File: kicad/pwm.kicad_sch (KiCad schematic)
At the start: 27 parts, among them J28 DC ports, J29 LED ports, J30 PCA9685 #1 ch 0, Q11 AO3400A, U7 PCA9685PW, U8 74HCT244D, U9 74HCT244D

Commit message: kicad: v2 space measures - feeder on power bar header, resistor arrays, 0603, TSSOP buffers
Feeder port dropped: power bar header pin 10 = +3V3_EXT (own AMS1117), any PCA #2 channel as signal; 30 series resistors as 8x 4x0603 arrays; new passives 0603; new 74HCT244 in TSSOP-20; flat parts may use the Pi zone, connectors anywhere else. ERC 0, DRC copper 0, parity 0.

Co-Authored-By: Claude Opus 5.5 <noreply@anthropic.com>
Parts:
- removed D29: SS54, Diode_SMD:D_SMA, symbol Device:D_Schottky
- removed J30: PCA9685 #1 ch 0, aquaPCB:TerminalBlock_Kangnex_WJ250B-3.5-03P_P3.50mm_Staggered, symbol Connector:Screw_Terminal_01x03
- removed Q11: AO3400A, Package_TO_SOT_SMD:SOT-23, symbol Transistor_FET:AO3400A
- removed R53, R54, R55, R56, R57, R58, R59, R60, R61, R62, R63, R64, R65, R66, R67: 100, Resistor_SMD:R_0805_2012Metric, symbol Device:R
- removed R68: 10k, Resistor_SMD:R_0805_2012Metric, symbol Device:R
- added RN1, RN2, RN3, RN4: 4x100, Resistor_SMD:R_Array_Convex_4x0603, symbol Device:R_Pack04
- C20, C21, C22: footprint Capacitor_SMD:C_0805_2012Metric -> Capacitor_SMD:C_0603_1608Metric; LCSC C49678 -> C14663
- U8, U9: value 74HCT244D -> 74HCT244PW; footprint Package_SO:SOIC-20W_7.5x12.8mm_P1.27mm -> Package_SO:TSSOP-20_4.4x6.5mm_P0.65mm; LCSC C5978 -> C131088
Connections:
- net DC_PWM1: now also RN1.8 (R1.2)
- net DC_PWM1_B: now also RN1.1 (R1.1)
- net DC_PWM2: now also RN1.7 (R2.2)
- net DC_PWM2_B: now also RN1.2 (R2.1)
- net DC_PWM3: now also RN1.6 (R3.2)
- net DC_PWM3_B: now also RN1.3 (R3.1)
- net DC_PWM4: now also RN1.5 (R4.2)
- net DC_PWM4_B: now also RN1.4 (R4.1)
- net DC_PWM6: now also RN2.8 (R1.2)
- net DC_PWM6_B: now also RN2.1 (R1.1)
- net DC_PWM7: now also RN2.7 (R2.2)
- net DC_PWM7_B: now also RN2.2 (R2.1)
- net DC_PWM9: now also RN2.6 (R3.2)
- net DC_PWM9_B: now also RN2.3 (R3.1)
- net LED_PWM10: now also RN3.7 (R2.2)
- net LED_PWM10_B: now also RN3.2 (R2.1)
- net LED_PWM11: now also RN3.6 (R3.2)
- net LED_PWM11_B: now also RN3.3 (R3.1)
- net LED_PWM12: now also RN3.5 (R4.2)
- net LED_PWM12_B: now also RN3.4 (R4.1)
- net LED_PWM13: now also RN4.8 (R1.2)
- net LED_PWM13_B: now also RN4.1 (R1.1)
- net LED_PWM14: now also RN4.7 (R2.2)
- net LED_PWM14_B: now also RN4.2 (R2.1)
- net LED_PWM15: now also RN4.6 (R3.2)
- net LED_PWM15_B: now also RN4.3 (R3.1)
- net LED_PWM8: now also RN3.8 (R1.2)
- net LED_PWM8_B: now also RN3.1 (R1.1)
- net PCA1_CH0: no longer names the net of U7.6 (LED0)
- no-connect marks 3 -> 8
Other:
- note added: "PCA9685 #1, I2C address 0x40. /OE fixed to GND: after power-on all outputs are LOW (datasheet 7.5); a Pi reboot does NOT reset the chip - outputs keep their state until software re-initialises it. LED0, LED5 = spare."
- note removed: "Feeder (Robo-Tank v3 order +3.3V / Signal / GND; Signal = switched ground, < 500 mA)"
- note removed: "PCA9685 #1, I2C address 0x40. /OE fixed to GND: after power-on all outputs are LOW (datasheet 7.5); a Pi reboot does NOT reset the chip - outputs keep their state until software re-initialises it. LED5 = spare."

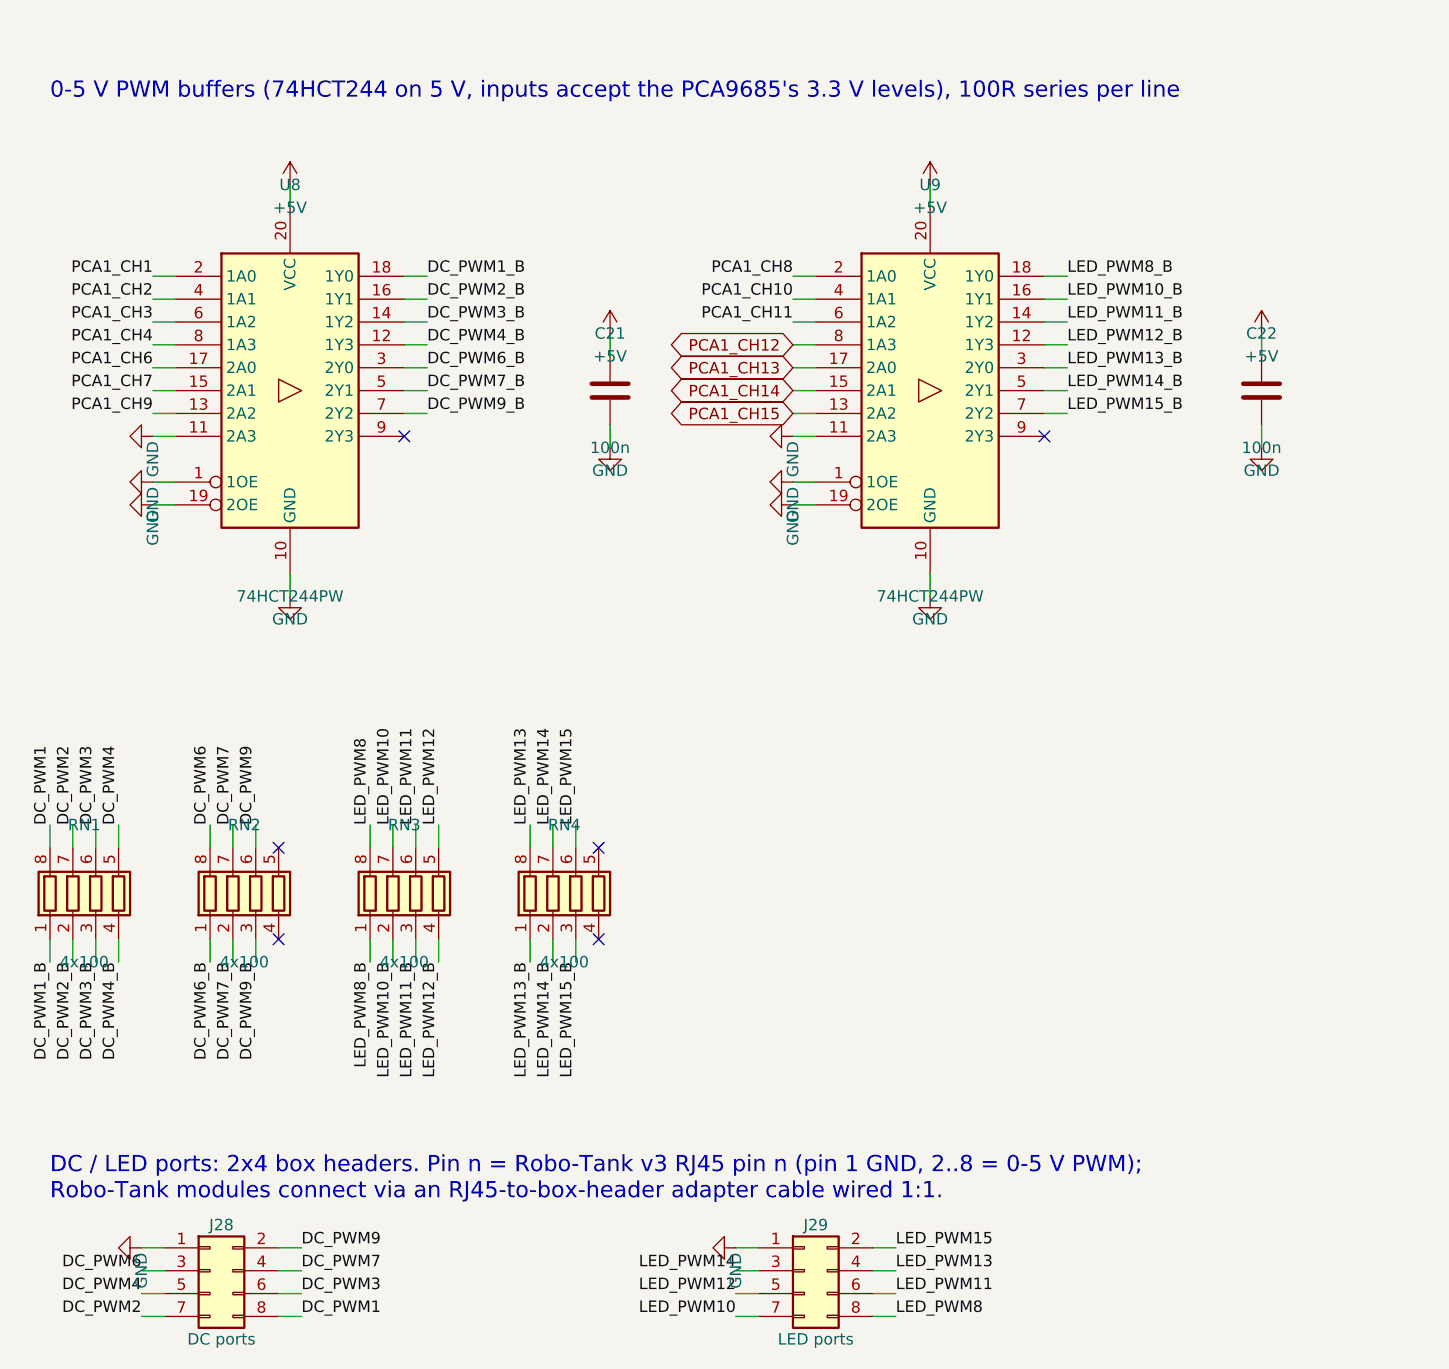
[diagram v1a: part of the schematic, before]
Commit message: kicad: pin headers for 1-Wire, ADC and floats; connectivity-driven re-placement
J19, ADC sockets (J36/J37/J26/J27, 3x4 grid) and floats J30/J31 are pin headers now. All footprints placed on the board (big connectors first, flat parts allowed under the Pi, user-placed U10/RN5/J32/U11 and user routing kept): signal ratsnest 7824 -> 4450 mm, crossings 1776 -> 862. ERC 0, DRC copper 0, parity 0.

Co-Authored-By: Claude Opus 5.5 <noreply@anthropic.com>
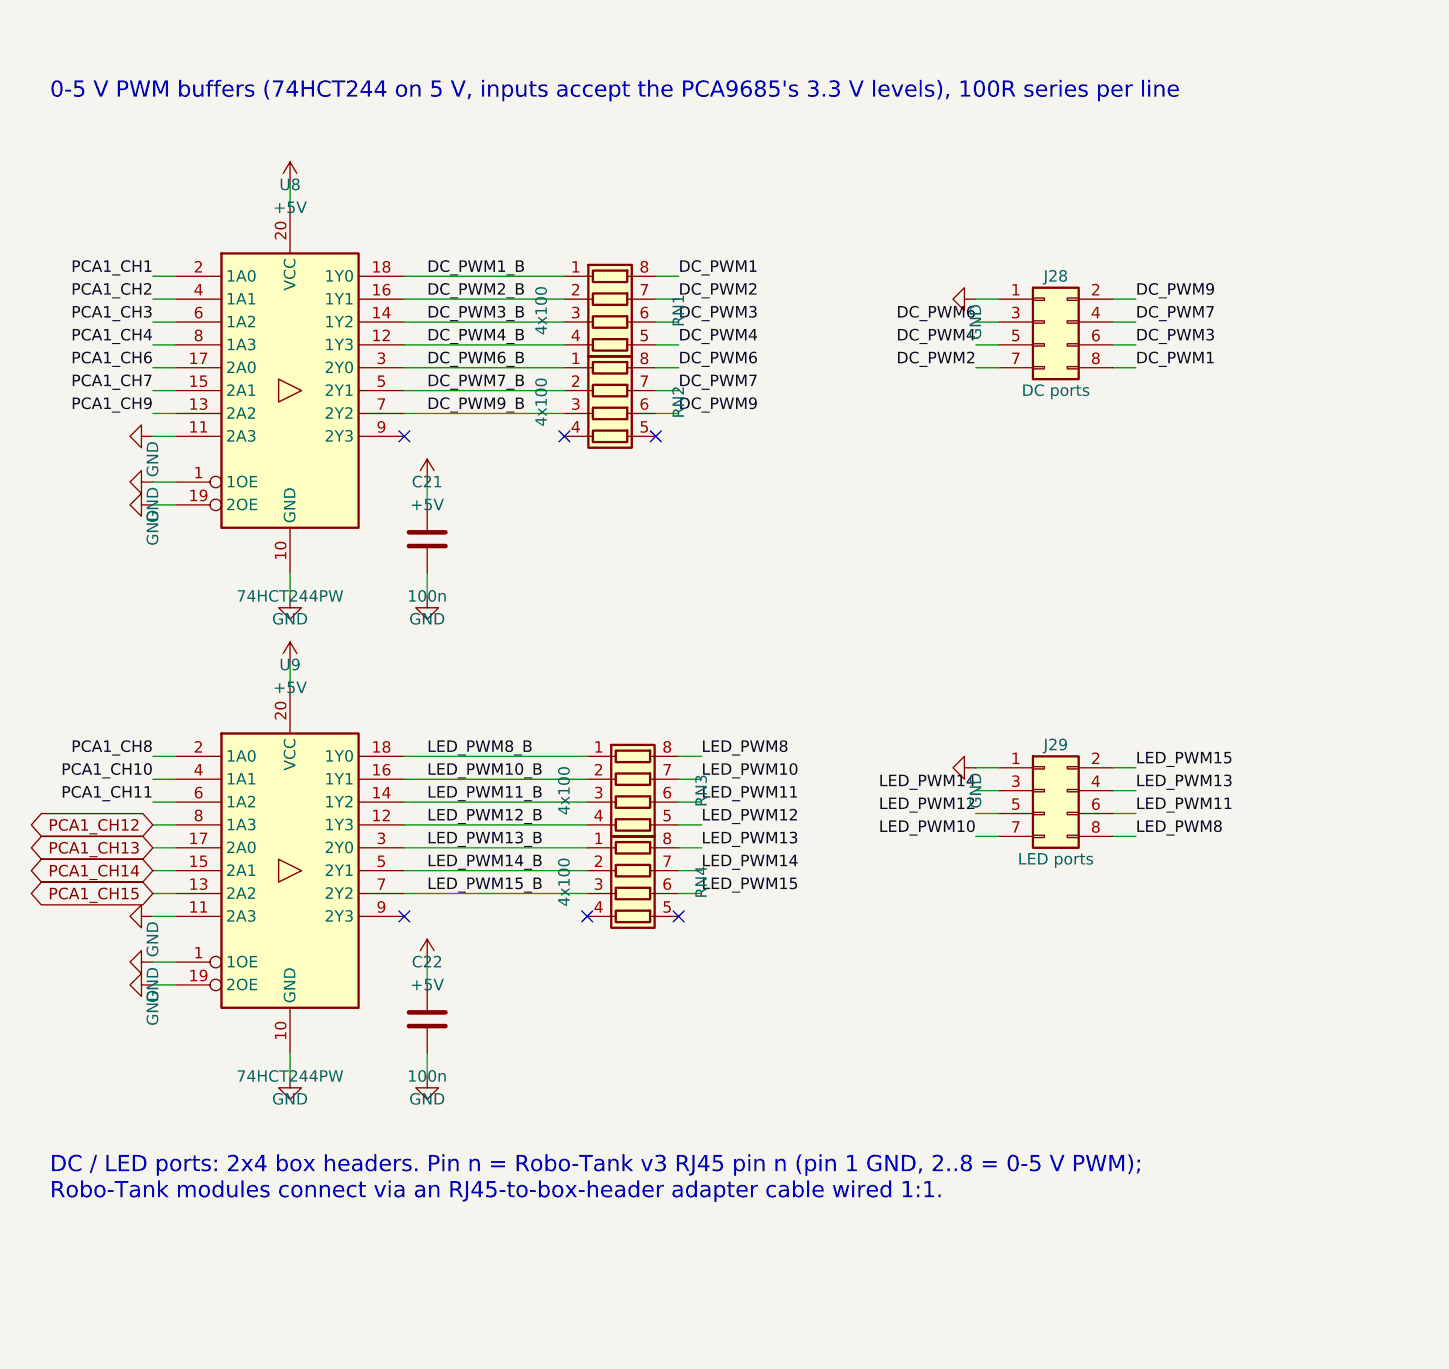
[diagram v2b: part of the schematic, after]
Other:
- moved on the sheet: C21, C22, J28, J29, RN1, RN2, RN3, RN4, U9

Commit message: kicad: PWM #1 group placed and routed, supply and signal routing
- PWM #1 (PCA9685 #1, 74HCT244 buffers, RN1..RN4, DC/LED ports): placed
  on the board clear of the Pi mounting hole H5, J29 fully on the board;
  all internal nets routed. Identical buffer gates and array elements
  re-assigned to cut crossings (PCA9685 channel -> port unchanged);
  pwm.kicad_sch relaid out with a label stub per buffer/array pin.
- Floats: J30/J31 and R53/R54 swapped, re-routed.
- Routing of +3V3, +3V3_EXT, +5V_EXT, I2C, sensor inputs and the PCA1
  CH12..15 links to the power section.
- Fixes: PCA1_CH14 break closed, stray vias/stubs removed, clearance
  violations at J2, R7 and along SDA resolved, J32 pin 9 thermal relief
  restored; C10 nudged and F2/C2/C12 references moved off pads.

Co-Authored-By: Claude Opus 5.5 <noreply@anthropic.com>
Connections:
- net DC_PWM1: now also RN2.7 (R2.2); no longer RN1.8 (R1.2)
- net DC_PWM1_B: now also RN2.2 (R2.1), U8.7 (2Y2); no longer RN1.1 (R1.1), U8.18 (1Y0)
- net DC_PWM2: now also RN2.8 (R1.2); no longer RN1.7 (R2.2)
- net DC_PWM2_B: now also RN2.1 (R1.1), U8.3 (2Y0); no longer RN1.2 (R2.1), U8.16 (1Y1)
- net DC_PWM3: now also RN2.6 (R3.2); no longer RN1.6 (R3.2)
- net DC_PWM3_B: now also RN2.3 (R3.1), U8.5 (2Y1); no longer RN1.3 (R3.1), U8.14 (1Y2)
- net DC_PWM4: now also RN1.8 (R1.2); no longer RN1.5 (R4.2)
- net DC_PWM4_B: now also RN1.1 (R1.1), U8.18 (1Y0); no longer RN1.4 (R4.1), U8.12 (1Y3)
- net DC_PWM6: now also RN1.6 (R3.2); no longer RN2.8 (R1.2)
- net DC_PWM6_B: now also RN1.3 (R3.1), U8.14 (1Y2); no longer RN2.1 (R1.1), U8.3 (2Y0)
- net DC_PWM7: now also RN1.7 (R2.2); no longer RN2.7 (R2.2)
- net DC_PWM7_B: now also RN1.2 (R2.1), U8.16 (1Y1); no longer RN2.2 (R2.1), U8.5 (2Y1)
- net DC_PWM9: now also RN1.5 (R4.2); no longer RN2.6 (R3.2)
- net DC_PWM9_B: now also RN1.4 (R4.1), U8.12 (1Y3); no longer RN2.3 (R3.1), U8.7 (2Y2)
- net LED_PWM10: now also RN3.3 (R3.1); no longer RN3.7 (R2.2)
- net LED_PWM10_B: now also RN3.6 (R3.2); no longer RN3.2 (R2.1)
- net LED_PWM11: now also RN3.2 (R2.1); no longer RN3.6 (R3.2)
- net LED_PWM11_B: now also RN3.7 (R2.2); no longer RN3.3 (R3.1)
- net LED_PWM12: now also RN4.6 (R3.2); no longer RN3.5 (R4.2)
- net LED_PWM12_B: now also RN4.3 (R3.1), U9.3 (2Y0); no longer RN3.4 (R4.1), U9.12 (1Y3)
- net LED_PWM13: now also RN3.1 (R1.1); no longer RN4.8 (R1.2)
- net LED_PWM13_B: now also RN3.8 (R1.2), U9.12 (1Y3); no longer RN4.1 (R1.1), U9.3 (2Y0)
- net LED_PWM15: now also RN4.8 (R1.2); no longer RN4.6 (R3.2)
- net LED_PWM15_B: now also RN4.1 (R1.1); no longer RN4.3 (R3.1)
- net LED_PWM8: now also RN3.4 (R4.1); no longer RN3.8 (R1.2)
- net LED_PWM8_B: now also RN3.5 (R4.2); no longer RN3.1 (R1.1)
- net PCA1_CH1: now also U8.13 (2A2); no longer U8.2 (1A0)
- net PCA1_CH12: now also U9.17 (2A0); no longer U9.8 (1A3)
- net PCA1_CH13: now also U9.8 (1A3); no longer U9.17 (2A0)
- net PCA1_CH2: now also U8.17 (2A0); no longer U8.4 (1A1)
- net PCA1_CH3: now also U8.15 (2A1); no longer U8.6 (1A2)
- net PCA1_CH4: now also U8.2 (1A0); no longer U8.8 (1A3)
- net PCA1_CH6: now also U8.6 (1A2); no longer U8.17 (2A0)
- net PCA1_CH7: now also U8.4 (1A1); no longer U8.15 (2A1)
- net PCA1_CH9: now also U8.8 (1A3); no longer U8.13 (2A2)
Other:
- moved on the sheet: J28, J29, RN1, RN2, RN3, RN4

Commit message: kicad: v2 layout finished - ADC renumbering, port labels, last routes
- ADC sockets numbered 0..3 from right to left; AIN0<->AIN1 and AIN2<->AIN3
  swapped at the ADS1115, U5 end runs re-routed.
- Connector labels: IoRegistry-style port names (PCA#1 chNN, ADC #1 in n,
  GPIO n, DS1820); J5/J6/J8/J9 corrected from GPIO to PCA#1 ch15/14/13/12
  (also in outputs.kicad_sch). Back side: names with voltage/current
  ratings, running from the board edge at pin 1, "+" on supply pins,
  SCL/SDA and 1-Wire Data marks. Front: ADC #1 / in n, jumper labels.
- Routed the last six open nets (+3V3 at J24/JP4, +5V_EXT at J19,
  GPIO2_SDA J22-J23 on B.Cu, AIN1, J24 pin 10 - JP3, PCA1_CH1); PCA1_CH3
  partly moved to B.Cu to free the corridor at U7. Dangling stubs removed.
- Silkscreen: nothing on pads, overlaps reduced with small moves; part
  references and F.Fab texts at 0.8 mm.
- aquaPCB.kicad_dru: the deliberate courtyard overlap of the ADC socket
  pairs J26/J27 and J36/J37 (2.54 mm grid) is waived by a custom rule.

ERC clean, DRC without errors (silkscreen warnings only), board fully
routed and in sync with the schematic.

Co-Authored-By: Claude Opus 5.5 <noreply@anthropic.com>
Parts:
- C20, C21, C22: footprint Capacitor_SMD:C_0603_1608Metric -> Capacitor_SMD:C_0805_2012Metric; LCSC C14663 -> C49678
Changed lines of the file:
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@@
 			)
 		)
-		(property "Footprint" "Capacitor_SMD:C_0603_1608Metric"
+		(property "Footprint" "Capacitor_SMD:C_0805_2012Metric"
 			(at 67.31 220.98 0)
 			(hide yes)
@@
 			)
 		)
-		(property "LCSC" "C14663"
+		(property "LCSC" "C49678"
 			(at 67.31 220.98 0)
 			(hide yes)
@@
 			)
 		)
-		(property "Footprint" "Capacitor_SMD:C_0603_1608Metric"
+		(property "Footprint" "Capacitor_SMD:C_0805_2012Metric"
 			(at 99.06 74.93 0)
 			(hide yes)
@@
 			)
 		)
-		(property "LCSC" "C14663"
+		(property "LCSC" "C49678"
 			(at 99.06 74.93 0)
 			(hide yes)
@@
 			)
 		)
-		(property "Footprint" "Capacitor_SMD:C_0603_1608Metric"
+		(property "Footprint" "Capacitor_SMD:C_0805_2012Metric"
 			(at 67.31 167.64 0)
 			(hide yes)
@@
 			)
 		)
-		(property "LCSC" "C14663"
+		(property "LCSC" "C49678"
 			(at 67.31 167.64 0)
 			(hide yes)

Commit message: kicad: LCSC numbers for PCA9685 and PTC, status LED names follow PCA#1
- U7/U10 PCA9685PW,118 -> LCSC C2678753, F2 nSMD050 -> C69688 (schematic
  and board), so every assembled part carries an LCSC number.
- Status LEDs D9/D11/D15/D17 renamed GPIO12/13/16/26 -> PCA#1 ch15/14/13/12,
  matching the Q2/Q3/Q5/Q6 drive since v2.

Co-Authored-By: Claude Opus 5.5 <noreply@anthropic.com>
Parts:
- U7: LCSC (none) -> C2678753
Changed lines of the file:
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@@
+			)
+		)
+		(property "LCSC" "C2678753"
+			(at 58.42 73.66 0)
+			(hide yes)
+			(show_name no)
+			(do_not_autoplace no)
+			(effects
+				(font
+					(size 1.27 1.27)
+				)
 			)
 		)
